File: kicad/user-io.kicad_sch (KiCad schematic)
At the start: 3 parts, among them J3 Micro_SD_Card, J4 USB1, U3 MIMXRT1171DVMAB

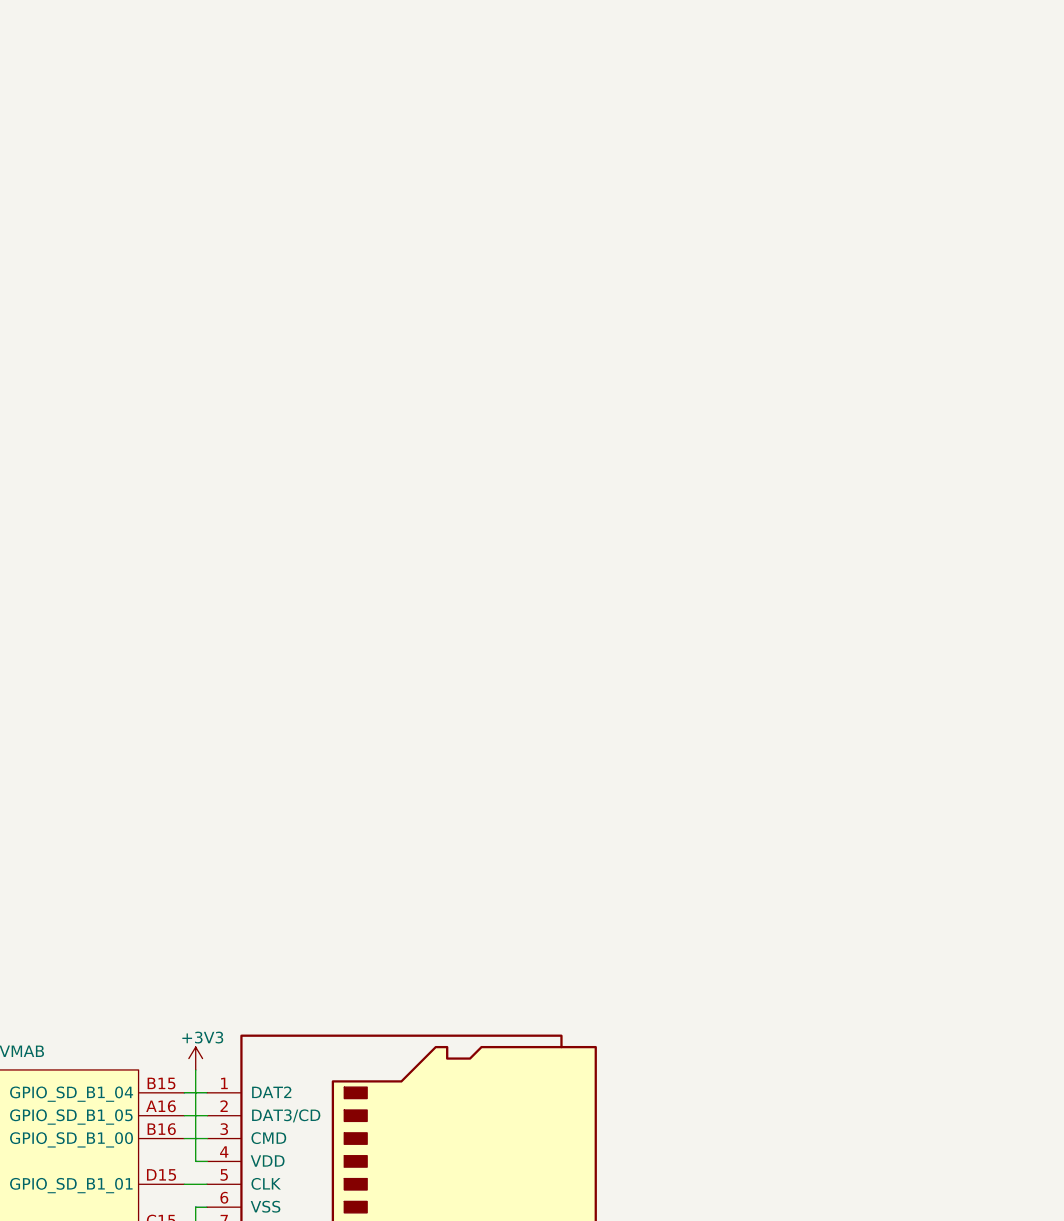
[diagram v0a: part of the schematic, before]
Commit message: added MAYA-W166-00B symbol
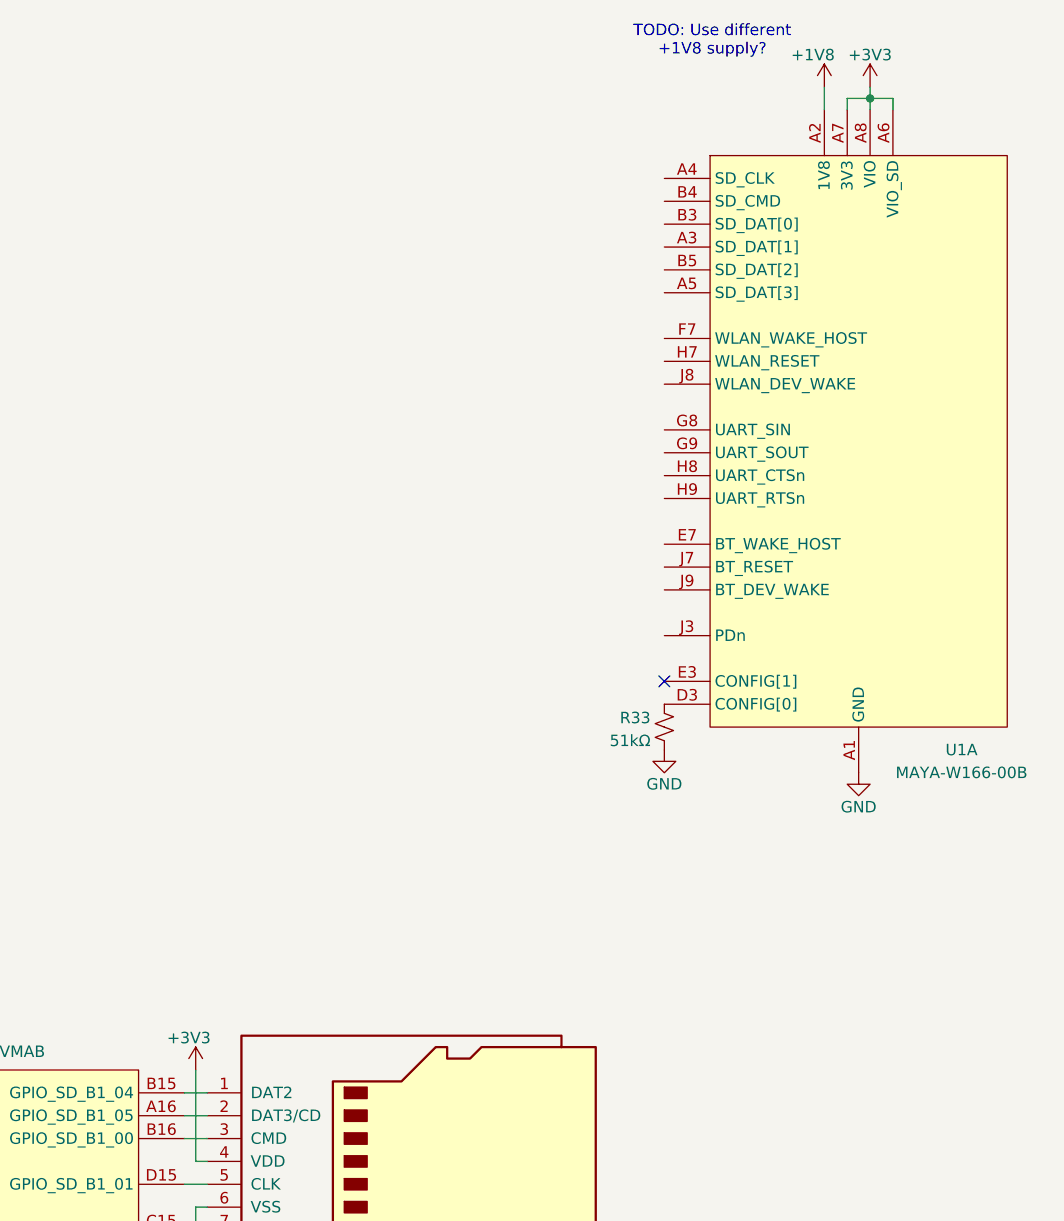
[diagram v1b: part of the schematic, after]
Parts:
- added R33: 51kΩ, symbol Device:R_Small_US
- added U1: MAYA-W166-00B, symbol project_symbols:MAYA-W166-00B
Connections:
- net +3V3: now also U1.A6 (VIO_SD), U1.A7 (3V3), U1.A8 (VIO), U1.B7 (3V3)
- net GND: now also R33.2, U1.A1 (GND), U1.A9 (GND), U1.B2 (GND), U1.B8 (GND), U1.E4 (GND), U1.E5 (GND), U1.F4 (GND), U1.F5 (GND), U1.H4 (GND), U1.H5 (GND), U1.K2 (GND), U1.K3 (GND), U1.K4 (GND), U1.K6 (GND), U1.K7 (GND), U1.K8 (GND), U1.L1 (GND), U1.L9 (GND), U1.M1 (GND), U1.M2 (GND), U1.M8 (GND), U1.M9 (GND)
- new net: R33.1, U1.D3 (CONFIG[0])
- new net +1V8: U1.A2 (1V8)
- no-connect marks 0 -> 1
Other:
- note added: "TODO: Use different +1V8 supply?"

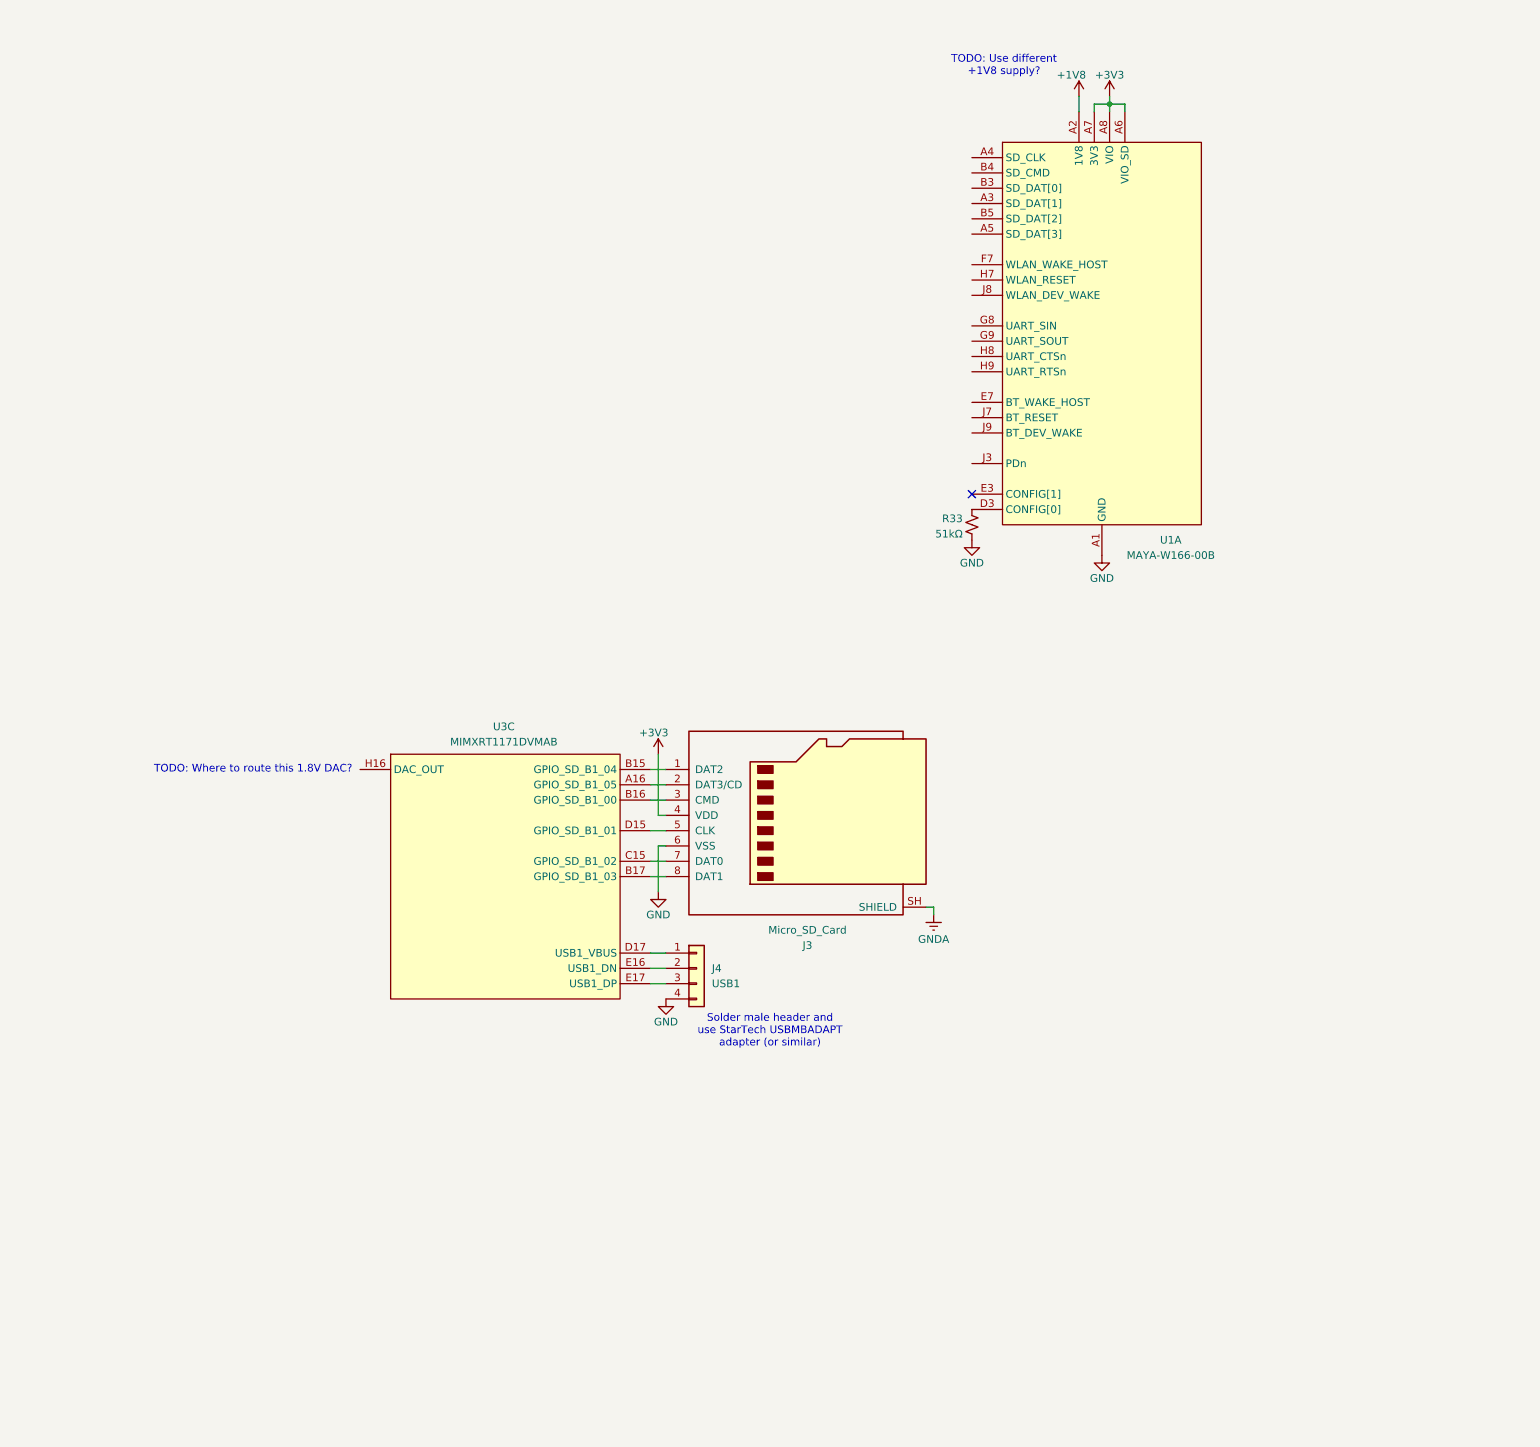
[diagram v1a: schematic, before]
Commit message: reworked design to use 1.8V logic
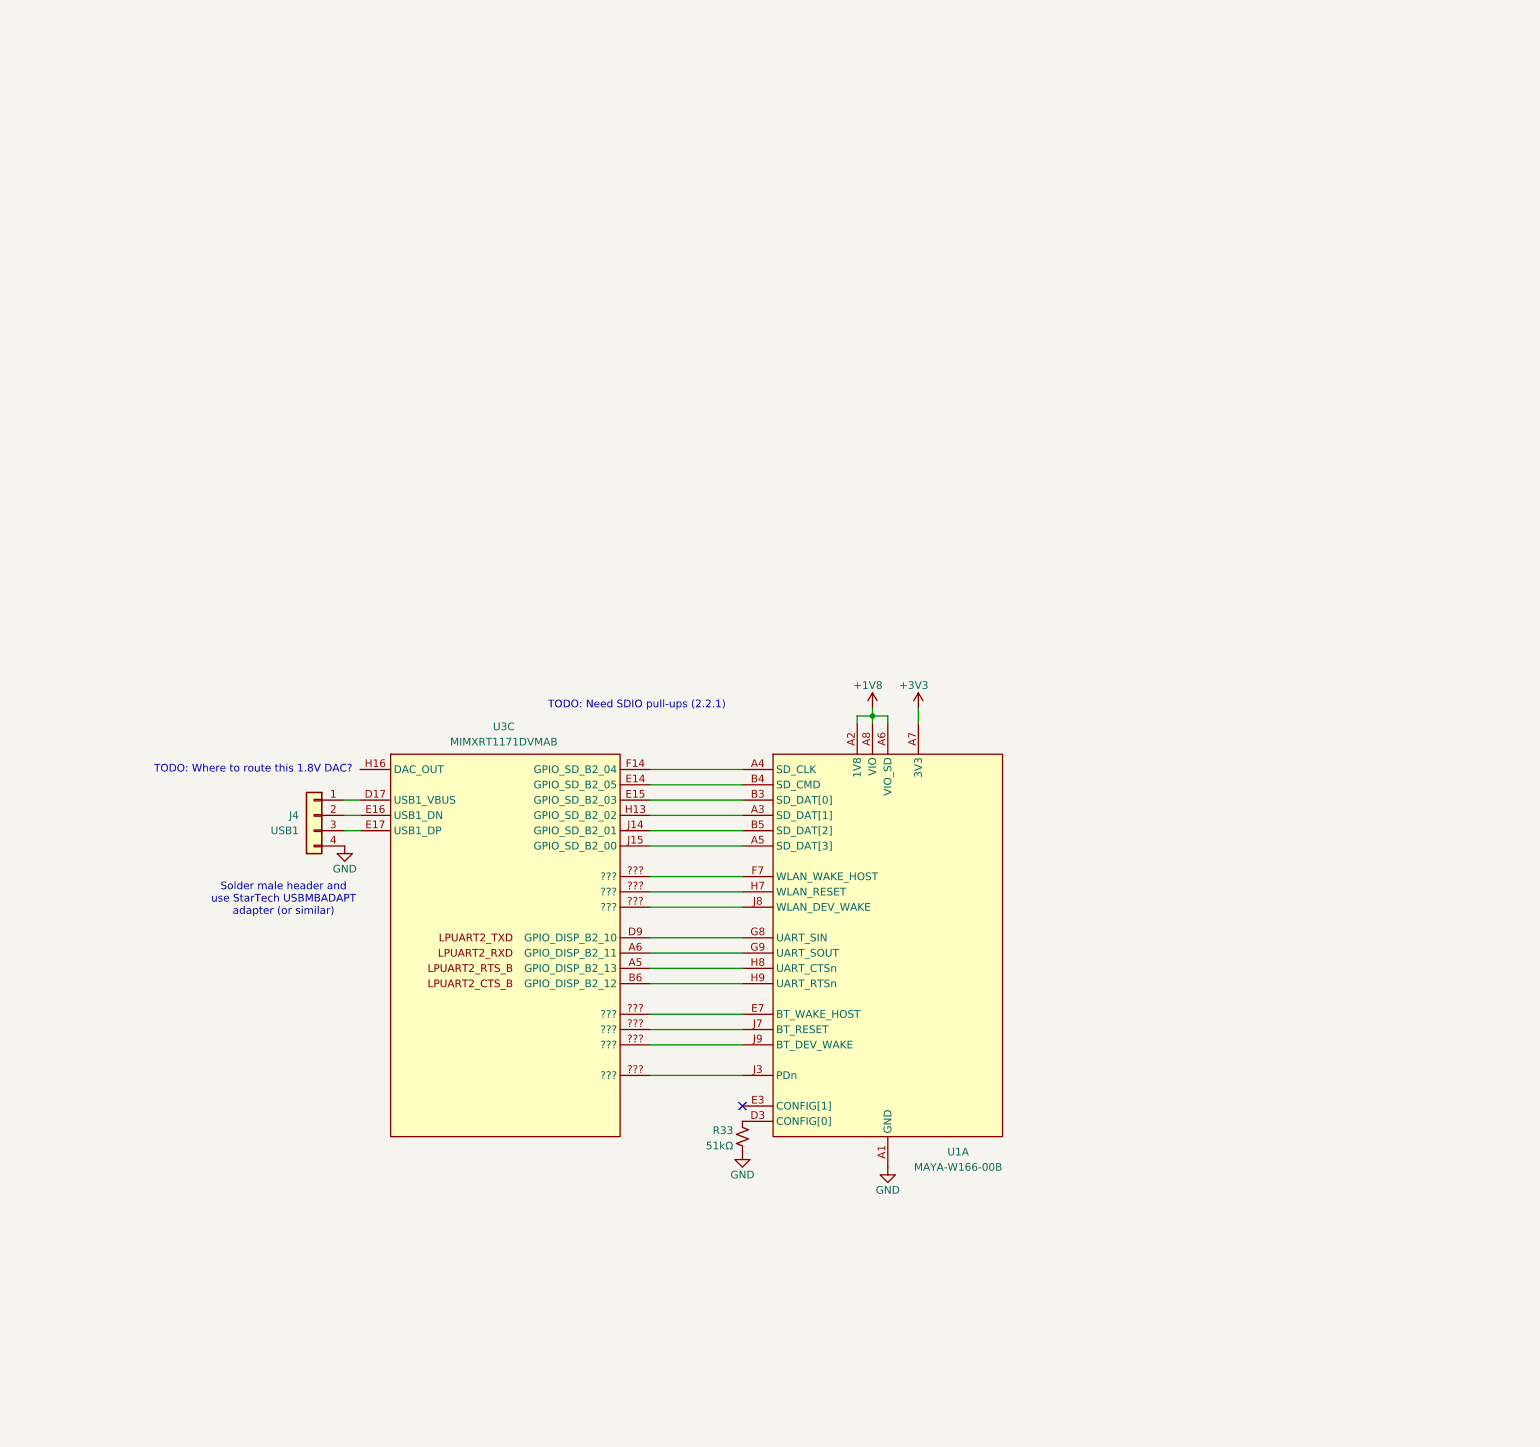
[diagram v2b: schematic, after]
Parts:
- removed J3: Micro_SD_Card, symbol Connector:Micro_SD_Card
- U1: footprint (none) -> project_footprints:MAYA-W166-00B
- U3: footprint (none) -> Package_BGA:MAPBGA-289_14x14mm_Layout17x17_P0.8mm
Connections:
- net +1V8: now also U1.A6 (VIO_SD), U1.A8 (VIO)
- net +3V3: no longer U1.A6 (VIO_SD), U1.A8 (VIO)
- net at U1.A3 (SD_DAT[1]): now also U3.H13 (GPIO_SD_B2_02)
- net at U1.A4 (SD_CLK): now also U3.F14 (GPIO_SD_B2_04)
- net at U1.A5 (SD_DAT[3]): now also U3.J15 (GPIO_SD_B2_00)
- net at U1.B3 (SD_DAT[0]): now also U3.E15 (GPIO_SD_B2_03)
- net at U1.B4 (SD_CMD): now also U3.E14 (GPIO_SD_B2_05)
- net at U1.B5 (SD_DAT[2]): now also U3.J14 (GPIO_SD_B2_01)
- net at U1.E7 (BT_WAKE_HOST): now also U3.???
- net at U1.F7 (WLAN_WAKE_HOST): now also U3.???
- net at U1.G8 (UART_SIN): now also U3.D9 (GPIO_DISP_B2_10)
- net at U1.G9 (UART_SOUT): now also U3.A6 (GPIO_DISP_B2_11)
- net at U1.H7 (WLAN_RESET): now also U3.???
- net at U1.H8 (UART_CTSn): now also U3.A5 (GPIO_DISP_B2_13)
- net at U1.H9 (UART_RTSn): now also U3.B6 (GPIO_DISP_B2_12)
- net at U1.J3 (PDn): now also U3.???
- net at U1.J7 (BT_RESET): now also U3.???
- net at U1.J8 (WLAN_DEV_WAKE): now also U3.???
- net at U1.J9 (BT_DEV_WAKE): now also U3.???
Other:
- note added: "TODO: Need SDIO pull-ups (2.2.1)"
- note removed: "TODO: Use different +1V8 supply?"
- moved on the sheet: R33, U1A

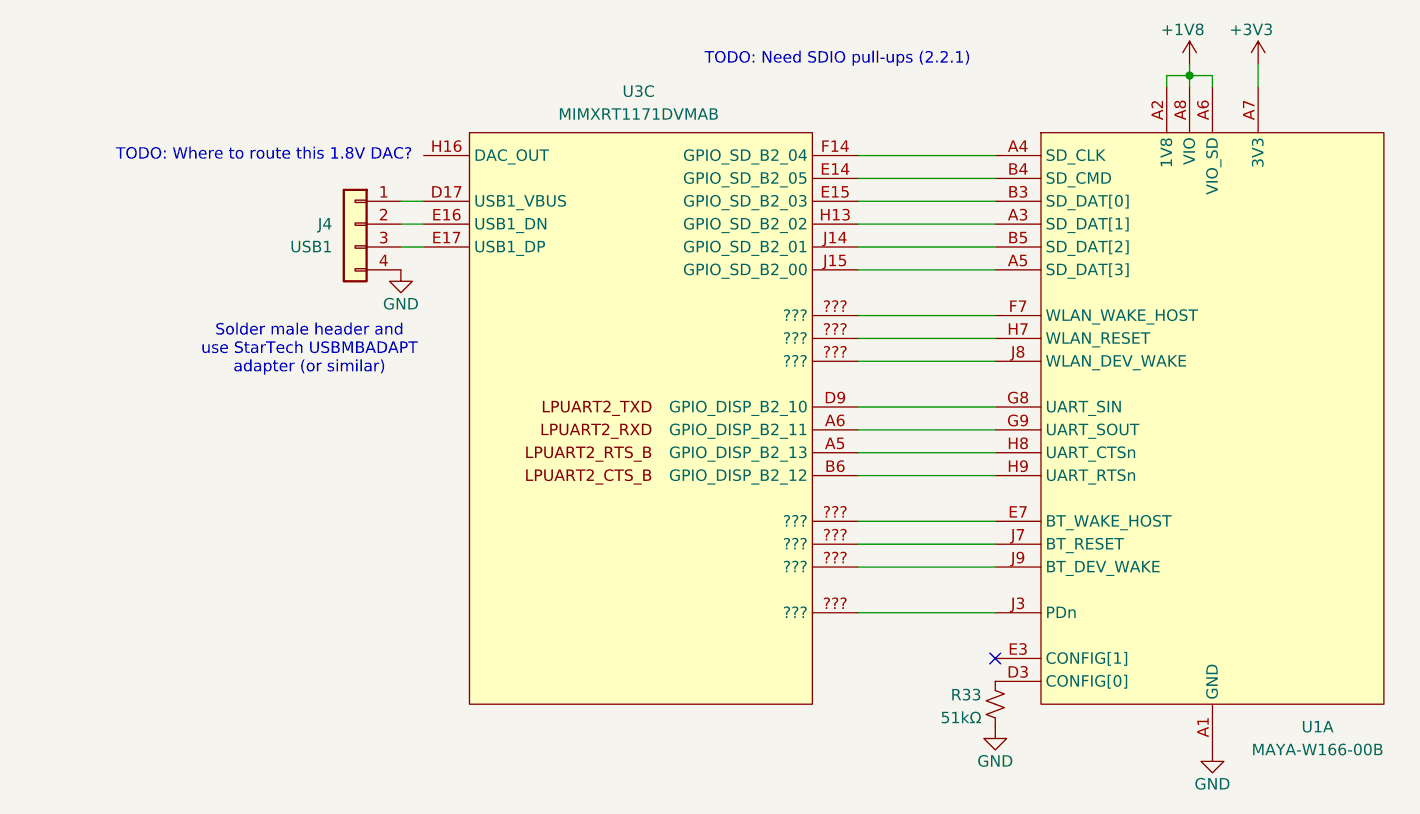
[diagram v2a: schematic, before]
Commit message: added user button and LED
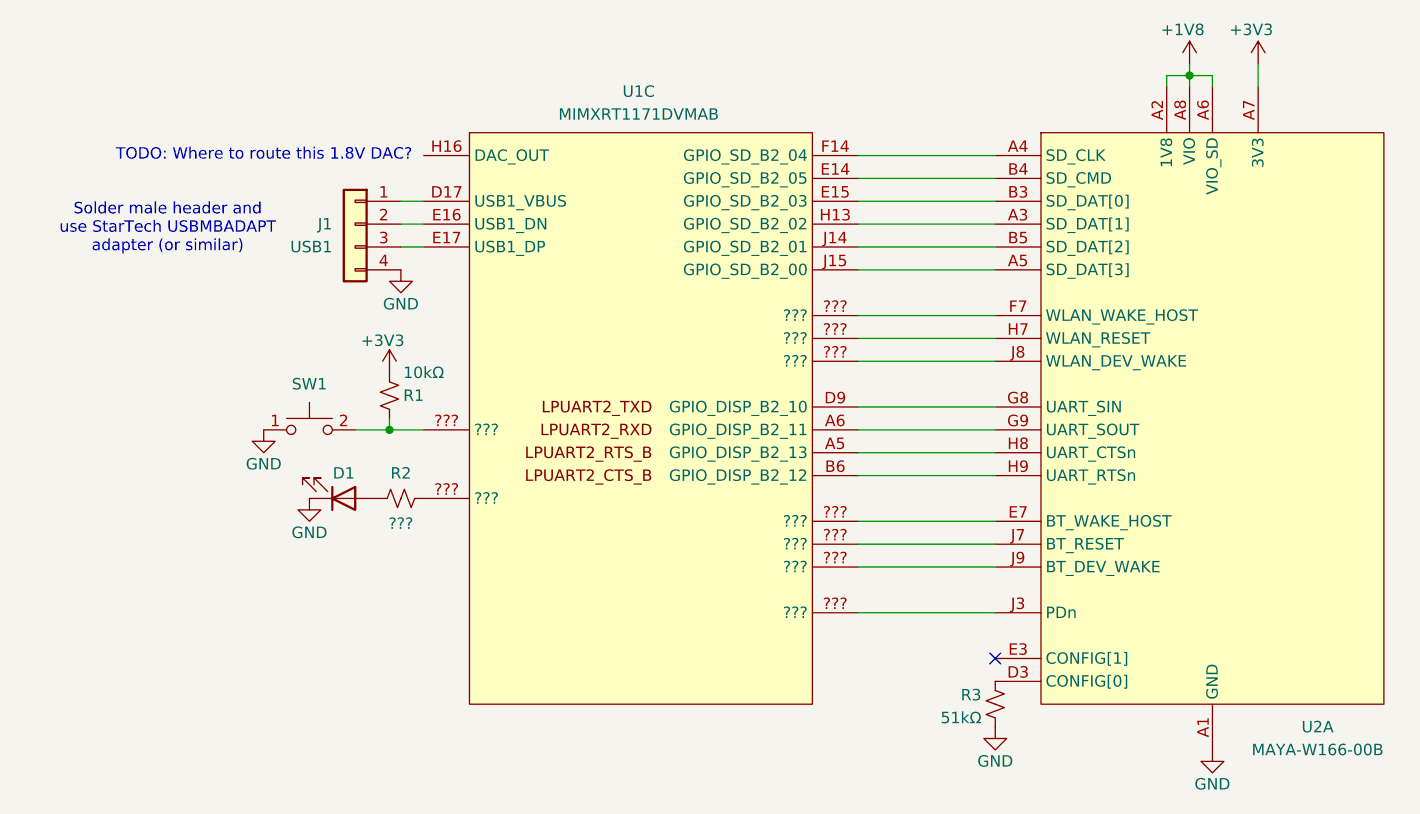
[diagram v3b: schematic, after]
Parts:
- added D1: RED, symbol Device:LED
- added R1: 10kΩ, symbol Device:R_Small_US
- added R2: ???, symbol Device:R_Small_US
- added SW1: PTS815, project_footprints:PTS815, symbol Switch:SW_Push
- renumbered J4 to J1, R33 to R3, U3 to U1, U1 to U2
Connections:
- net +3V3: now also R1.2
- net GND: now also D1.1 (K), SW1.1
- new net: R1.1, SW1.2, U1.???
- new net: D1.2 (A), R2.1
- new net: R2.2, U1.???
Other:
- note removed: "TODO: Need SDIO pull-ups (2.2.1)"
